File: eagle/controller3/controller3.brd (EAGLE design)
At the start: 55.9 x 50.8 mm, 37 parts, among them J1 FEMALE 2x3, J4 USB-MICROB

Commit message: controller3 update eagle files
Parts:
- removed C3: 100nF, SparkFun-Passives:CAP-PTH-SMALL
- removed R10, R11, R12: (no value), adafruit:R3225
- removed RES: (no value), SparkFun-FreqCtrl:RESONATOR-PTH
- removed U$1: ATMEGA32U4TQFP, SparkFun-Retired:SPARKFUN-DIGITALIC_TQFP44
- added C2: (no value), SparkFun-Capacitors:1206
- added C4, C5, R4, R9, RB1, RB2, RB3, RDISP, RRST, RTEMP, RUSB1, RUSB2, RZERO, VD5, VD6: (no value), SparkFun-Passives:1206
- added ICSP, ZERO: (no value), SparkFun-Connectors:2X3
- added Q1: (no value), adafruit:HC49U70
- added T_CAM1, T_CAM2: (no value), SparkFun-DiscreteSemi:TO-92
- added U$3: ATMEGA32U4-AU, adafruit:TQFP44
- J1: value FEMALE 2x3 -> (none); device SparkFun-Connectors:2X3 -> SparkFun-Connectors:1X02_LOCK
- R1, R2, R3, R8: device adafruit:R3225 -> SparkFun-Passives:1206
- VD1, VD2, VD3, VD4: device adafruit:R3216 -> SparkFun-Passives:1206
- moved U$2 54.7 mm to (16.5, 64.8), turned to 90 degrees
- moved TEMP 42.2 mm to (27.9, 5.08), turned to 270 degrees
- moved R1 33.6 mm to (29.2, 44.5), turned to 90 degrees
- moved R8 28.4 mm to (17.8, 10.2), turned to 90 degrees
- moved VD4 21.6 mm to (21.6, 36.8), turned to 180 degrees
- moved VD3 21.6 mm to (25.4, 36.8), turned to 270 degrees
- moved R2 21.3 mm to (20.3, 19.1), turned to 180 degrees
- moved R3 18.0 mm to (20.3, 25.4), turned to 180 degrees
- moved SH 17.1 mm to (30.5, 49.1)
- moved BTN_UP 15.3 mm to (52.1, 6.35), turned to 90 degrees
- moved VD2 15.3 mm to (21.6, 34.3), turned to 180 degrees
- moved MOSFET_CAM 15.2 mm to (25.4, 44.5), turned to 90 degrees
- moved BTN_X 14.0 mm to (36.8, 6.35), turned to 90 degrees
- moved VD1 12.7 mm to (25.4, 31.8), turned to 90 degrees
- moved C1 11.7 mm to (52.1, 26.7)
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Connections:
- removed net CAM_VCC: PWR_CAM.PWR
- removed net EXT_EN: U$1.30
- removed net N$7: J4.GND, J4.MT1, J4.MT2
- new net MISO: ICSP.1, U$3.11
- new net MOSI: ICSP.4, U$3.10
- new net N$12: RZERO.1, T_ZERO.2
- new net N$13: RDISP.2, T_DISP.2
- new net N$14: J4.D+, RUSB1.2
- new net N$15: J4.D-, RUSB2.2
- new net N$16: J3.TIP, SHTR.2, T_CAM1.1
- new net N$17: J3.SHIELD, SHTR.3, T_CAM2.1
- new net N$18: R2.2, T_CAM1.2
- new net N$19: R3.2, T_CAM2.2
- new net N$20: C2.2, U$3.6
- new net N$21: MOSFET_CAM.1, R1.2, R4.1
- new net N$23: U$3.26
- new net N$24: U$3.22
- new net N$28: U$3.12
- new net SCK: ICSP.3, U$3.9
- new net VD_DIRECT: U$3.28, VD5.1, VD6.2
- net BATT_VCC: now also PWR_CAM.PWR, VD5.2
- net BTN1: now also RB1.2, U$3.41; no longer R11.2, U$1.38
- net BTN2: now also RB2.2, U$3.40; no longer R8.2, U$1.39
- net BTN3: now also RB3.2, U$3.39; no longer R10.2, U$1.40
- net CAM1: now also R2.1, U$3.32; no longer J3.SHIELD, SHTR.3, U$1.32
- net CAM2: now also R3.1, U$3.31; no longer J3.TIP, SHTR.2, U$1.26
- net CAM_EN: now also R4.2, U$3.27; no longer MOSFET_CAM.1, U$1.12
- net CELL1: now also U$3.29, VD3.2; no longer U$1.37, VD1.2, VD2.1
- net CELL2: now also U$3.30, VD1.2, VD2.1; no longer U$1.36, VD3.2
- net DISP_EN: now also RDISP.1, U$3.37; no longer T_DISP.2, U$1.31
- net DISP_RST: now also U$3.36; no longer U$1.28
- net GND: now also BTN_DW.1, BTN_UP.1, BTN_X.1, C2.1, C4.1, C5.1, ICSP.6, J4.GND, J4.MT1, J4.MT2, R1.1, T_CAM1.3, T_CAM2.3, U$3.15, U$3.23, U$3.33, U$3.35, U$3.43, U$3.5, VD6.1, ZERO.4; no longer BTN_DW.2, BTN_UP.2, BTN_X.2, C3.1, J1.4, RES.2, U$1.15, U$1.23, U$1.35, U$1.43, U$1.5
- net N$1: now also RRST.1, U$3.13; no longer R12.2, U$1.13
- net N$10: now also ZERO.2; no longer J1.2
- net N$11: now also J1.1, U$3.7; no longer U$1.7
- net N$4: now also RUSB1.1, U$3.3; no longer J4.D-, U$1.3
- net N$5: now also RUSB2.1, U$3.4; no longer J4.D+, U$1.4
- net N$8: now also C4.2, Q1.2, U$3.17; no longer RES.3
- net N$9: now also C5.2, Q1.1, U$3.16; no longer RES.1
- net RST: now also ICSP.5, ZERO.6; no longer J1.6
- net RX: now also U$3.20, ZERO.3; no longer J1.3, U$1.20
- net SCL: now also R8.1, U$3.18; no longer R3.2, U$1.18
- net SDA: now also R9.2, U$3.19; no longer R1.1, U$1.19
- net TEMP: now also RTEMP.1, U$3.38; no longer R2.2, U$1.29
- net TX: now also U$3.21, ZERO.5; no longer J1.5, U$1.21
- net VCC: now also ICSP.2, J1.2, R8.2, R9.1, RB1.1, RB2.1, RB3.1, RRST.2, RTEMP.2, U$3.14, U$3.2, U$3.24, U$3.34, U$3.44, ZERO.1; no longer C3.2, J1.1, R1.2, R10.1, R11.1, R12.1, R2.1, R3.1, R8.1, U$1.14, U$1.24, U$1.34, U$1.42, U$1.44
- net ZERO_EN: now also RZERO.2, U$3.25; no longer T_ZERO.2, U$1.27
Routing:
- net TX: track 121.1 -> 0.00 mm
- net GND: track 208.9 -> 316.2 mm
- net MOSI: track 0.00 -> 58.5 mm
- net N$1: track 61.0 -> 7.89 mm, vias 4 -> 0
- net BATT_VCC: track 49.4 -> 94.4 mm, vias 0 -> 1
- net N$14: track 0.00 -> 36.0 mm
- net CAM1: track 47.1 -> 13.3 mm
- net N$10: track 36.3 -> 7.93 mm
- net DISP_RST: track 51.1 -> 25.6 mm
- net N$17: track 0.00 -> 25.4 mm
- net SDA: track 66.7 -> 41.6 mm, vias 2 -> 3
- net VCC: track 186.0 -> 161.2 mm
- net N$9: track 0.00 -> 22.0 mm
- net N$11: track 0.00 -> 21.6 mm, vias 0 -> 1
- net SCL: track 82.4 -> 61.0 mm, vias 2 -> 1
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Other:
- board size 55.9 x 50.8 mm -> 63.5 x 50.8 mm
- board text removed: "1"
- board text removed: "2"
- board text removed: "3.3V"
- board text removed: "5V"
- board text removed: "BALANCER"
- board text removed: "DISP"
- board text removed: "GND"
- board text removed: "MID"
- board text removed: "MOSFET CAM"
- board text removed: "SHTR"
- board text removed: "TIP"
- board text removed: "VCC"

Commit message: controller3: eagle files update
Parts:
- removed U$2: V_REG_LD1117VXX, SparkFun-PowerIC:78XXL
- added C3: 10uF, SparkFun-Passives:1206
- C1: device SparkFun-Passives:CAP-PTH-SMALL -> SparkFun-Passives:1206
- C2: value (none) -> 1uF
- Q1: device adafruit:HC49U70 -> adafruit:CTS406
- moved R8 37.7 mm to (44.5, 36.8)
- moved R9 37.7 mm to (41.9, 36.8)
- moved RTEMP 9.25 mm to (29.2, 12.7), turned to 0 degrees
- moved J1 5.08 mm to (47.0, 19.1)
- moved ZERO 4.02 mm to (50.8, 43.2)
- moved RUSB2 4.02 mm to (49.5, 15.2), turned to 0 degrees
- moved T_DISP 4.02 mm to (17.8, 11.4)
- moved RDISP 3.81 mm to (24.1, 10.2)
- moved U$3 3.81 mm to (34.3, 24.1)
- moved C2 3.59 mm to (53.3, 16.5)
- moved BTN_DW 2.54 mm to (41.9, 6.35)
- moved BTN_UP 2.54 mm to (49.5, 6.35)
- moved BTN_X 2.54 mm to (34.3, 6.35)
- moved CONV_X_VCC 2.54 mm to (57.1, 30.5)
- moved H2 2.54 mm to (57.1, 3.81)
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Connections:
- new net N$22: C3.1, J4.VBUS
- net N$11: now also C3.2; no longer J4.VBUS
- net N$8: now also Q1.3; no longer Q1.2
- net VCC: now also DISP.6; no longer DISP.5
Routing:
- net SDA: track 41.6 -> 85.9 mm, vias 3 -> 2
- net TX: track 0.00 -> 35.5 mm
- net N$14: track 36.0 -> 4.84 mm
- net GND: track 316.2 -> 285.3 mm, vias 3 -> 2
- net MOSI: track 58.5 -> 32.4 mm, vias 0 -> 1
- net BATT_VCC: track 94.4 -> 72.7 mm, vias 1 -> 2
- net SCL: track 61.0 -> 71.5 mm, vias 1 -> 2
- net BTN2: track 25.8 -> 19.9 mm, vias 1 -> 0
- net N$1: track 7.89 -> 12.8 mm
- net RST: track 33.0 -> 37.3 mm
- net N$11: track 21.6 -> 25.5 mm, vias 1 -> 0
- net N$9: track 22.0 -> 24.8 mm
- net N$5: track 14.9 -> 12.3 mm, vias 2 -> 0
- net VCC: track 161.2 -> 158.7 mm
- net ZERO_EN: track 19.9 -> 22.3 mm
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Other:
- board size 63.5 x 50.8 mm -> 61 x 50.8 mm

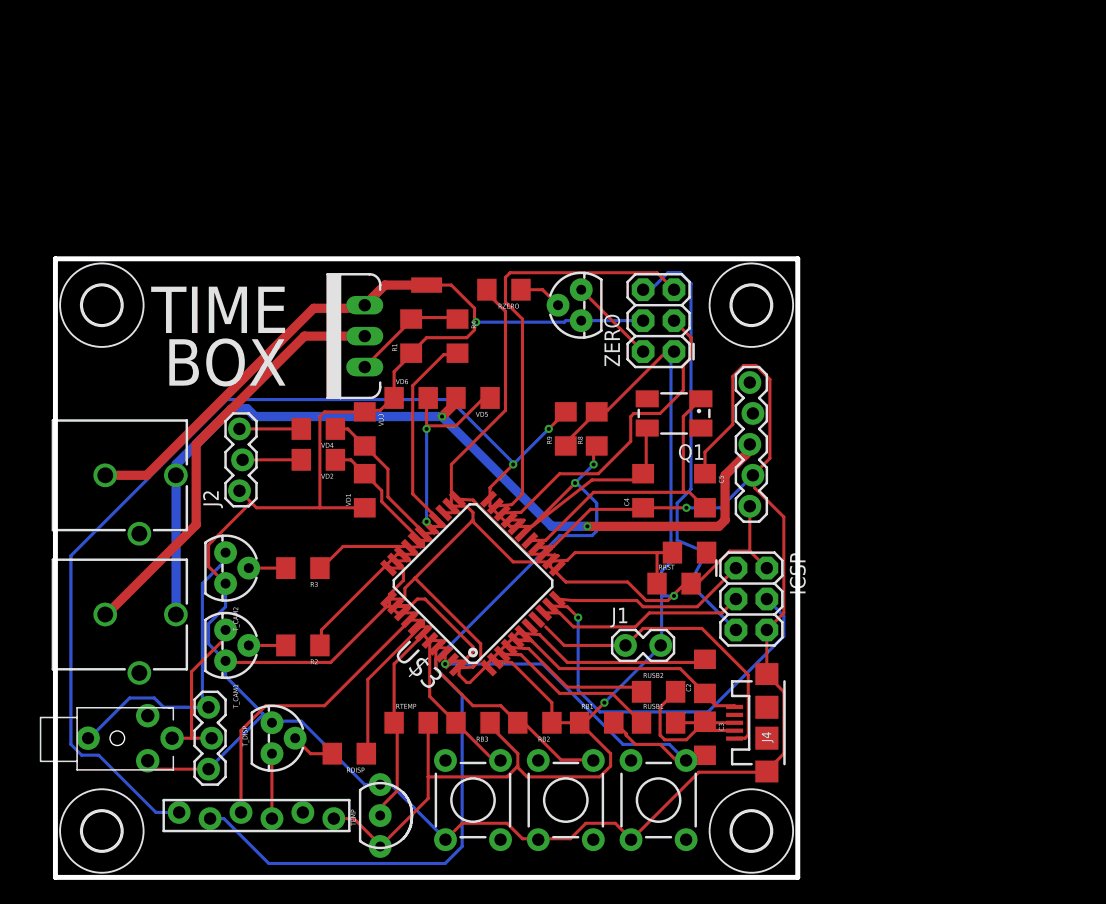
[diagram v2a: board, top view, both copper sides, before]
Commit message: controller 2.4 / 3.0 changes
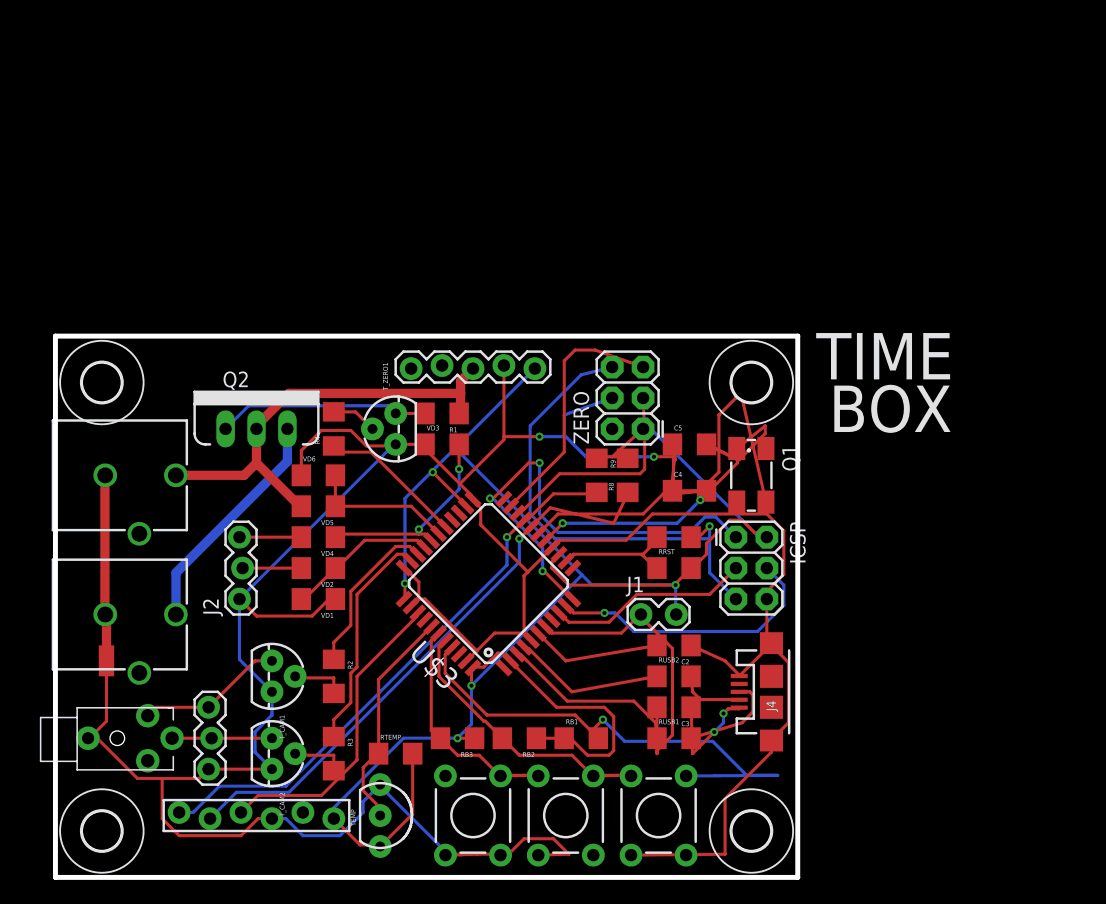
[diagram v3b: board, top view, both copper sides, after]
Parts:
- removed MOSFET_CAM: (no value), SparkFun-DiscreteSemi:TO220V
- removed RDISP, RZERO: (no value), SparkFun-Passives:1206
- removed T_DISP, T_ZERO: (no value), SparkFun-DiscreteSemi:TO-92
- added Q2: (no value), SparkFun-DiscreteSemi:TO220V
- added T_ZERO1: (no value), SparkFun-DiscreteSemi:TO-92
- U$3: value ATMEGA32U4-AU -> (none)
- moved SH 40.5 mm to (4.19, 17.8), turned to 270 degrees
- moved CONV_X_VCC 21.1 mm to (39.4, 41.9), turned to 180 degrees
- moved T_CAM2 15.7 mm to (17.8, 10.2)
- moved VD5 15.5 mm to (21.6, 30.5)
- moved R3 15.5 mm to (22.9, 10.2), turned to 270 degrees
- moved R4 12.7 mm to (22.9, 36.8), turned to 90 degrees
- moved VD6 9.92 mm to (21.6, 33.0)
- moved VD1 9.67 mm to (21.6, 22.9), turned to 180 degrees
- moved J2 8.89 mm to (15.2, 22.9)
- moved VD2 8.89 mm to (21.6, 25.4)
- moved VD4 8.89 mm to (21.6, 27.9)
- moved Q1 8.13 mm to (57.1, 33.0), turned to 270 degrees
- moved R1 6.84 mm to (31.8, 38.1), turned to 180 degrees
- moved ZERO 6.84 mm to (48.3, 36.8)
- moved VD3 6.48 mm to (31.8, 35.6), turned to 0 degrees
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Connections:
- removed net N$12: RZERO.1, T_ZERO.2
- removed net N$13: RDISP.2, T_DISP.2
- removed net N$6: DISP.4, T_DISP.3
- new net N$7: R4.2, T_ZERO1.2
- net BATT_VCC: now also Q2.2, R1.1; no longer PWR_CAM.PWR
- net CAM1: now also U$3.31; no longer U$3.32
- net CAM2: now also U$3.32; no longer U$3.31
- net CAM_EN: now also R4.1; no longer R4.2
- net CAM_OUT: now also PWR_CAM.PWR, Q2.3; no longer MOSFET_CAM.2, PWR_CAM.GND
- net DISP_EN: no longer RDISP.1
- net GND: now also DISP.4, J3.SHIELD, T_ZERO1.1; no longer J3.RING1, R1.1, T_DISP.1, T_ZERO.1
- net GNDA: now also PWR_CAM.GND; no longer MOSFET_CAM.3
- net N$10: no longer T_ZERO.3
- net N$16: now also J3.RING, SHTR.3; no longer J3.TIP, SHTR.2
- net N$17: now also J3.TIP, SHTR.2; no longer J3.SHIELD, SHTR.3
- net N$21: now also Q2.1, T_ZERO1.3; no longer MOSFET_CAM.1, R4.1
- net ZERO_EN: no longer RZERO.2
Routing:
- net SDA: track 85.9 -> 46.6 mm, vias 2 -> 1
- net BATT_VCC: track 72.7 -> 37.3 mm, vias 2 -> 0
- net N$8: track 15.5 -> 42.0 mm
- net SCL: track 71.5 -> 47.8 mm, vias 2 -> 1
- net MISO: track 16.2 -> 38.8 mm, vias 0 -> 3
- net ZERO_EN: track 22.3 -> 0.00 mm
- net GNDA: track 32.2 -> 14.7 mm
- net N$17: track 25.1 -> 8.20 mm
- net CAM_OUT: track 34.6 -> 19.0 mm
- net TX: track 35.5 -> 20.8 mm
- net DISP_EN: track 14.1 -> 0.00 mm
- net BTN1: track 33.0 -> 43.0 mm
- net N$22: track 0.00 -> 9.69 mm, vias 0 -> 2
- net MOSI: track 32.4 -> 23.3 mm
- net RX: track 26.8 -> 17.8 mm
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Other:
- board size 61 x 50.8 mm -> 61 x 44.5 mm

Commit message: controller3: changed board layout for milling
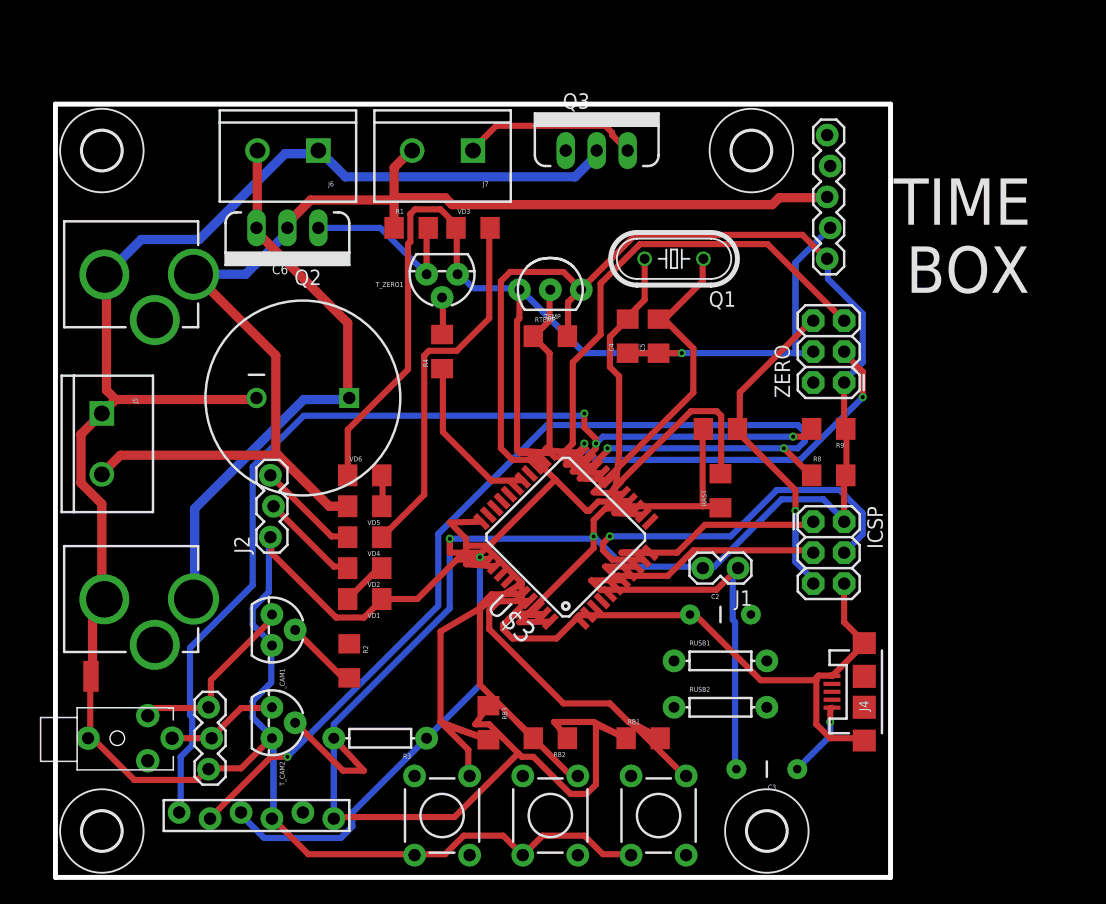
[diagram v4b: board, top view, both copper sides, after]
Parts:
- added C6: (no value), SparkFun-Capacitors:CPOL-RADIAL-1000UF-63V
- added J5, J6, J7: (no value), SparkFun-Connectors:SCREWTERMINAL-5MM-2
- added Q3: MOSFET-NCHANNELFQP30N06L, SparkFun-DiscreteSemi:TO220V
- C2: device SparkFun-Capacitors:1206 -> SparkFun-Capacitors:CAP-PTH-5MM
- C3: device SparkFun-Passives:1206 -> SparkFun-Passives:CAP-PTH-5MM
- PWR_BATT, PWR_CAM: value (none) -> POWER_JACKPTH_LOCK; device SparkFun-Connectors:POWER_JACK_PTH_BREAD -> SparkFun-Connectors:POWER_JACK_PTH_LOCK
- Q1: device adafruit:CTS406 -> adafruit:HC49/S
- R3, RUSB1, RUSB2: device SparkFun-Passives:1206 -> SparkFun-Passives:AXIAL-0.3
- moved TEMP 45.4 mm to (40.6, 48.3), turned to 0 degrees
- moved RTEMP 36.6 mm to (40.6, 44.5)
- moved CONV_X_VCC 25.7 mm to (63.5, 50.8), turned to 90 degrees
- moved R9 19.4 mm to (63.5, 36.8), turned to 180 degrees
- moved H1 19.0 mm to (3.81, 59.7)
- moved H3 19.0 mm to (57.1, 59.7)
- moved Q1 18.9 mm to (50.8, 50.8), turned to 180 degrees
- moved VD3 18.0 mm to (34.3, 53.3)
- moved ZERO 16.9 mm to (64.8, 40.6)
- moved Q2 16.7 mm to (19.1, 53.3), turned to 180 degrees
- moved PWR_BATT 16.6 mm to (-2.54, 49.5)
- moved R8 16.5 mm to (63.5, 33.0), turned to 0 degrees
- moved R1 15.5 mm to (29.2, 53.3), turned to 0 degrees
- moved C4 13.7 mm to (47.0, 44.5), turned to 90 degrees
- moved T_ZERO1 13.3 mm to (31.8, 49.5), turned to 180 degrees
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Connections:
- removed net N$23: U$3.26
- removed net N$24: U$3.22
- new net EXT_EN: Q3.1, U$3.26
- new net EXT_OUT: J7.1, Q3.3
- new net FOO: U$3.38
- net BATT_VCC: now also J5.2, J7.2
- net CAM2: now also R3.P$1; no longer R3.1
- net CAM_OUT: now also C6.1, J6.2
- net GNDA: now also C6.2, J5.1, J6.1, Q3.2
- net N$14: now also RUSB1.P$2; no longer RUSB1.2
- net N$15: now also RUSB2.P$2; no longer RUSB2.2
- net N$19: now also R3.P$2; no longer R3.2
- net N$4: now also RUSB1.P$1; no longer RUSB1.1
- net N$5: now also RUSB2.P$1; no longer RUSB2.1
- net N$8: now also Q1.2; no longer Q1.3
- net TEMP: now also U$3.22; no longer U$3.38
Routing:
- net GNDA: track 14.7 -> 93.5 mm
- net BATT_VCC: track 37.3 -> 102.9 mm
- net VCC: track 167.4 -> 228.7 mm, vias 5 -> 2
- net SCL: track 47.8 -> 92.1 mm, vias 1 -> 3
- net SDA: track 46.6 -> 86.7 mm, vias 1 -> 3
- net CAM_OUT: track 19.0 -> 47.6 mm
- net N$8: track 42.0 -> 20.3 mm
- net TX: track 20.8 -> 42.1 mm
- net MISO: track 38.8 -> 19.1 mm, vias 3 -> 0
- net CAM2: track 18.5 -> 0.00 mm
- net GND: track 276.8 -> 294.9 mm, vias 2 -> 1
- net RX: track 17.8 -> 34.9 mm, vias 0 -> 2
- net DISP_RST: track 25.5 -> 40.7 mm, vias 0 -> 1
- net N$4: track 14.9 -> 0.00 mm
- net EXT_OUT: track 0.00 -> 14.6 mm
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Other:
- board size 61 x 44.5 mm -> 68.6 x 63.5 mm

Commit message: bulk commit (eagle files, old changes)
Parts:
- C2: device SparkFun-Capacitors:CAP-PTH-5MM -> SparkFun-Capacitors:1206
- C3: device SparkFun-Passives:CAP-PTH-5MM -> SparkFun-Passives:1206
- R3, RUSB1, RUSB2: device SparkFun-Passives:AXIAL-0.3 -> SparkFun-Passives:1206
- moved VD3 31.7 mm to (15.2, 27.9), turned to 270 degrees
- moved J2 17.3 mm to (3.81, 17.8)
- moved VD1 17.3 mm to (8.89, 17.8)
- moved VD2 17.3 mm to (8.89, 20.3)
- moved VD4 17.3 mm to (8.89, 22.9)
- moved ZERO 17.1 mm to (52.1, 52.1)
- moved CONV_X_VCC 15.9 mm to (55.9, 64.8), turned to 180 degrees
- moved R9 15.3 mm to (52.1, 47.0)
- moved R8 15.3 mm to (52.1, 43.2)
- moved C5 14.0 mm to (63.5, 45.7), turned to 180 degrees
- moved C4 13.7 mm to (59.7, 49.5), turned to 180 degrees
- moved RRST 11.7 mm to (62.2, 40.6)
- moved Q1 10.9 mm to (61.0, 54.6)
- moved SH 10.2 mm to (2.92, 26.7)
- moved H3 9.16 mm to (64.8, 64.8)
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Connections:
- removed net N$14: J4.D+, RUSB1.P$2
- removed net N$15: J4.D-, RUSB2.P$2
- removed net N$22: C3.1, J4.VBUS
- new net N$12: J4.D-, RUSB1.2
- new net N$13: J4.D+, RUSB2.2
- new net N$6: C3.1, J4.VBUS, U$3.2
- net CAM2: now also R3.1; no longer R3.P$1
- net N$19: now also R3.2; no longer R3.P$2
- net N$4: now also RUSB1.1; no longer RUSB1.P$1
- net N$5: now also RUSB2.1; no longer RUSB2.P$1
- net VCC: no longer U$3.2
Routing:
- net TX: track 42.1 -> 0.00 mm
- net DISP_RST: track 40.7 -> 0.00 mm, vias 1 -> 0
- net RX: track 34.9 -> 0.00 mm, vias 2 -> 0
- net CELL2: track 3.96 -> 34.4 mm, vias 0 -> 2
- net GND: track 294.9 -> 324.0 mm, vias 1 -> 0
- net N$1: track 17.7 -> 46.8 mm
- net EXT_EN: track 0.00 -> 28.7 mm
- net N$6: track 0.00 -> 28.6 mm, vias 0 -> 2
- net N$4: track 0.00 -> 25.0 mm
- net BTN1: track 31.8 -> 7.21 mm
- net CAM2: track 0.00 -> 23.3 mm
- net BTN3: track 27.9 -> 4.79 mm
- net CAM1: track 0.00 -> 17.3 mm
- net N$5: track 0.00 -> 14.8 mm
- net N$20: track 0.00 -> 14.1 mm
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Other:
- board size 68.6 x 63.5 mm -> 68.6 x 68.6 mm
